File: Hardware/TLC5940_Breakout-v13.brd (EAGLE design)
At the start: 59.7 x 26.7 mm, 51 parts, among them U1 TLC5940-RHB, U2 V_REG_MIC52055V

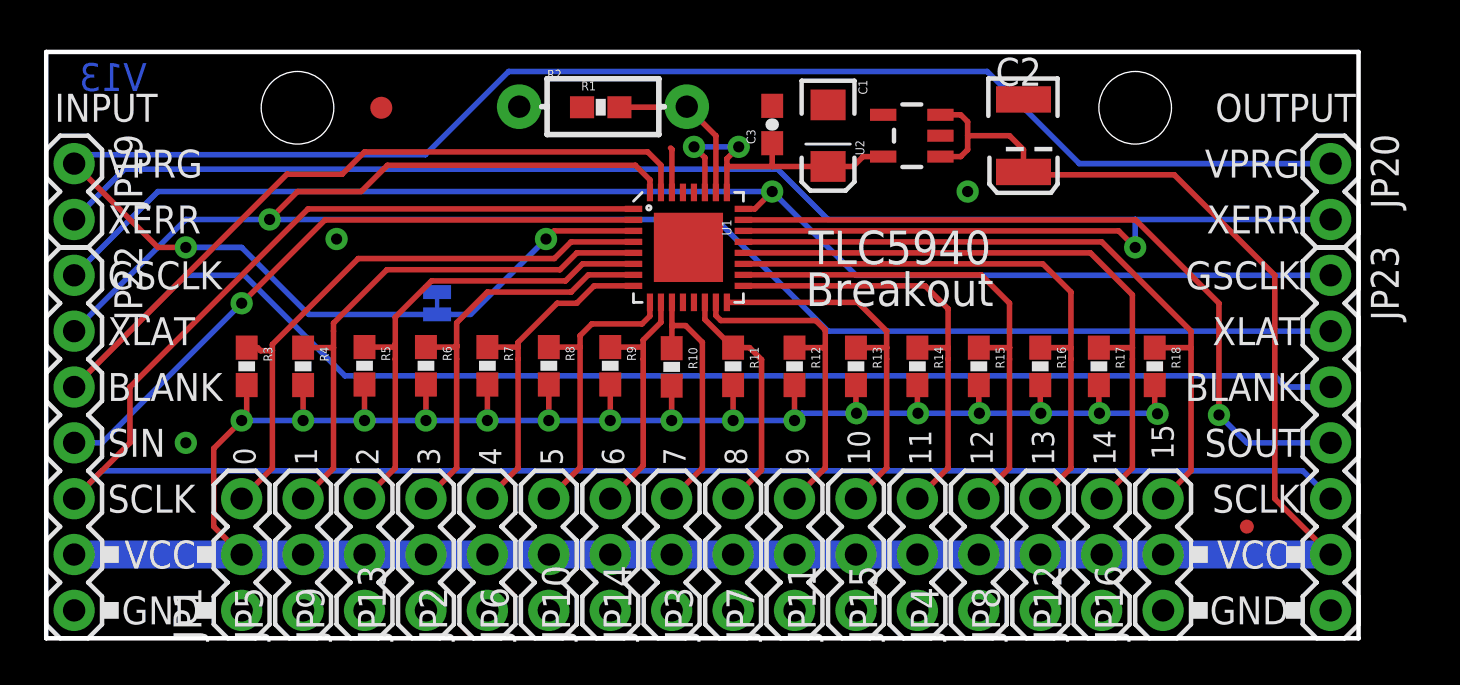
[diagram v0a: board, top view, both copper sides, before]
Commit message: Fixed sch issues, updated to 0603, minor re routes.
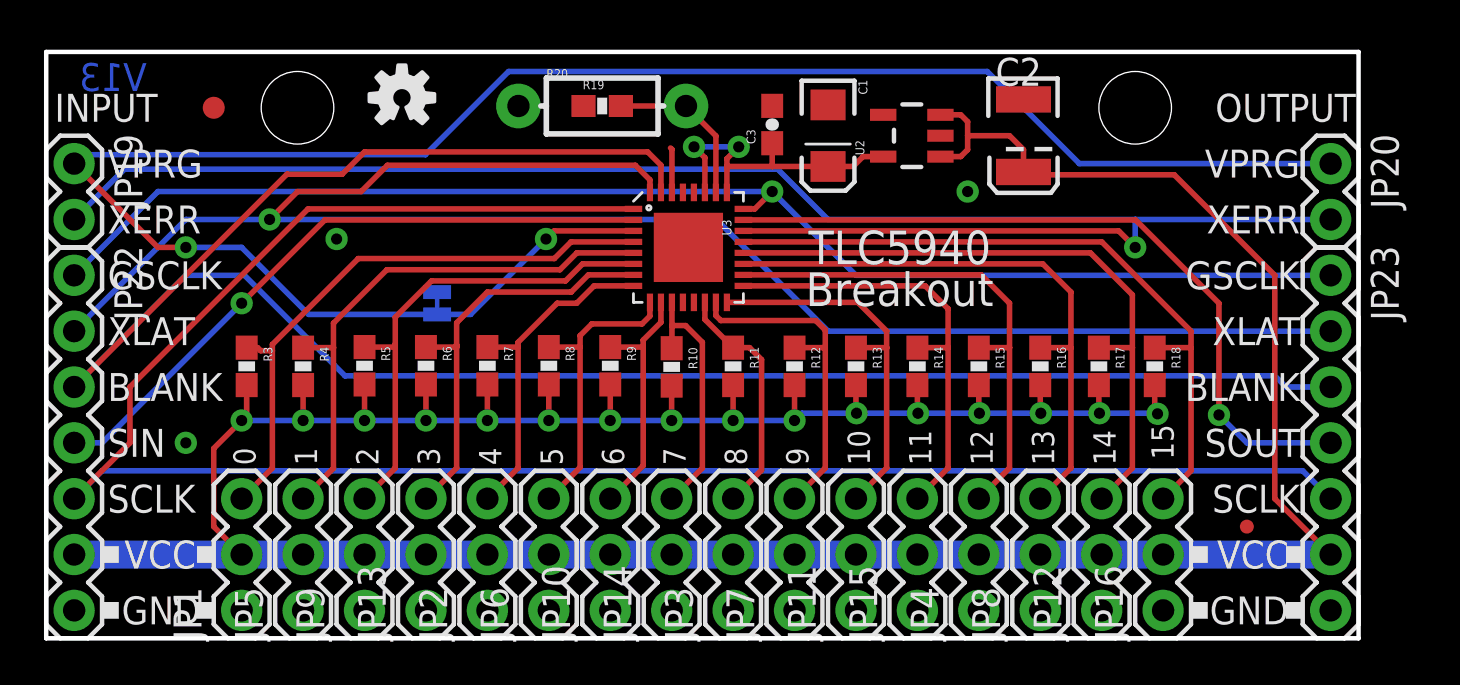
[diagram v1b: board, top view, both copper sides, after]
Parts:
- removed R1: 2.2k, SparkFun-Resistors:0603-RES
- removed R2: R2, SparkFun-Resistors:AXIAL-0.3-KIT
- removed U1: TLC5940-RHB, SparkFun:QFN-32
- added R19: 2.2k, SparkFun-Resistors:0603-RES
- added R20: R2, SparkFun-Resistors:AXIAL-0.3-KIT
- added U3: TLC5940-RHB, SparkFun-DigitalIC:QFN-32
- moved LOGO1 41.3 mm to (16.2, 24.6), flipped to the top
- moved JP26 7.62 mm to (7.62, 24.1)
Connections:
- removed net N$8: R1.2, R2.P$2, U1.26
- new net N$1: R19.2, R20.P$2, U3.26
- net 5V: now also U3.25, U3.27; no longer U1.25, U1.27
- net BLANK: now also U3.31; no longer U1.31
- net GND: now also R19.1, R20.P$1, U3.30; no longer R1.1, R2.P$1, U1.30
- net GSCLK: now also U3.24; no longer U1.24
- net OUT0: now also U3.4; no longer U1.4
- net OUT1: now also U3.5; no longer U1.5
- net OUT10: now also U3.16; no longer U1.16
- net OUT11: now also U3.17; no longer U1.17
- net OUT12: now also U3.18; no longer U1.18
- net OUT13: now also U3.19; no longer U1.19
- net OUT14: now also U3.20; no longer U1.20
- net OUT15: now also U3.21; no longer U1.21
- net OUT2: now also U3.6; no longer U1.6
- net OUT3: now also U3.7; no longer U1.7
- net OUT4: now also U3.8; no longer U1.8
- net OUT5: now also U3.9; no longer U1.9
- net OUT6: now also U3.10; no longer U1.10
- net OUT7: now also U3.11; no longer U1.11
- net OUT8: now also U3.14; no longer U1.14
- net OUT9: now also U3.15; no longer U1.15
- net SCLK: now also U3.1; no longer U1.1
- net SIN: now also U3.2; no longer U1.2
- net SOUT: now also U3.23; no longer U1.23
- net VPRG: now also U3.3; no longer U1.3
- net XERR: now also U3.22; no longer U1.22
- net XLAT: now also U3.32; no longer U1.32
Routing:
- net N$8: track 7.52 -> 0.00 mm
- net N$1: track 0.00 -> 7.46 mm

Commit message: Fixed QC Checklist issues
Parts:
- removed JP27: FIDUCIAL1X2.5, abes:FIDUCIAL-1X2.5
- added JP21: FIDUCIAL1X2, SparkFun:FIDUCIAL-1X2
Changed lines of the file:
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@@
 <setting verticaltext="up"/>
 </settings>
-<grid distance="0.05" unitdist="inch" unit="inch" style="lines" multiple="1" display="yes" altdistance="0.0001" altunitdist="inch" altunit="inch"/>
+<grid distance="0.05" unitdist="inch" unit="inch" style="lines" multiple="1" display="yes" altdistance="0.005" altunitdist="inch" altunit="inch"/>
 <layers>
 <layer number="1" name="Top" color="4" fill="1" visible="yes" active="yes"/>
@@
 <layer number="45" name="Holes" color="7" fill="1" visible="yes" active="yes"/>
 <layer number="46" name="Milling" color="3" fill="1" visible="no" active="yes"/>
-<layer number="47" name="Measures" color="7" fill="1" visible="yes" active="yes"/>
+<layer number="47" name="Measures" color="7" fill="1" visible="no" active="yes"/>
 <layer number="48" name="Document" color="7" fill="1" visible="no" active="yes"/>
 <layer number="49" name="Reference" color="7" fill="1" visible="no" active="yes"/>
@@
 <layer number="56" name="wert" color="7" fill="1" visible="no" active="yes"/>
 <layer number="57" name="tCAD" color="7" fill="1" visible="no" active="no"/>
+<layer number="59" name="tCarbon" color="7" fill="1" visible="no" active="no"/>
+<layer number="60" name="bCarbon" color="7" fill="1" visible="no" active="no"/>
 <layer number="90" name="Modules" color="5" fill="1" visible="no" active="yes"/>
 <layer number="91" name="Nets" color="2" fill="1" visible="no" active="no"/>
@@
 <layer number="127" name="_tValues" color="7" fill="1" visible="no" active="yes"/>
 <layer number="128" name="_bValues" color="7" fill="1" visible="no" active="yes"/>
+<layer number="129" name="Mask" color="7" fill="1" visible="yes" active="yes"/>
 <layer number="131" name="tAdjust" color="7" fill="1" visible="no" active="yes"/>
 <layer number="132" name="bAdjust" color="7" fill="1" visible="no" active="yes"/>
@@
 <layer number="223" name="223bmp" color="24" fill="1" visible="no" active="no"/>
 <layer number="224" name="224bmp" color="25" fill="1" visible="no" active="no"/>
+<layer number="225" name="225bmp" color="7" fill="1" visible="yes" active="yes"/>
+<layer number="226" name="226bmp" color="7" fill="1" visible="yes" active="yes"/>
+<layer number="227" name="227bmp" color="7" fill="1" visible="yes" active="yes"/>
+<layer number="228" name="228bmp" color="7" fill="1" visible="yes" active="yes"/>
+<layer number="229" name="229bmp" color="7" fill="1" visible="yes" active="yes"/>
+<layer number="230" name="230bmp" color="7" fill="1" visible="yes" active="yes"/>
+<layer number="231" name="231bmp" color="7" fill="1" visible="yes" active="yes"/>
 <layer number="248" name="Housing" color="7" fill="1" visible="no" active="yes"/>
 <layer number="249" name="Edge" color="7" fill="1" visible="no" active="yes"/>
@@
 </element>
 <element name="JP26" library="SparkFun" package="FIDUCIAL-1X2" value="FIDUCIAL1X2" x="7.62" y="24.13"/>
-<element name="JP27" library="abes" package="FIDUCIAL-1X2.5" value="FIDUCIAL1X2.5" x="54.61" y="5.08"/>
 <element name="FRAME1" library="SparkFun-Aesthetics" package="CREATIVE_COMMONS" value="FRAME-LETTER" x="-2.54" y="-16.51"/>
 <element name="LOGO1" library="SparkFun-Aesthetics" package="OSHW-LOGO-S" value="OSHW-LOGOS" x="16.1798" y="24.5872"/>
@@
 <attribute name="NAME" x="22.748240625" y="25.48128125" size="0.4064" layer="25" font="vector"/>
 </element>
+<element name="JP21" library="SparkFun" package="FIDUCIAL-1X2" value="FIDUCIAL1X2" x="54.61" y="5.08"/>
 </elements>
 <signals>
@@
 <contactref element="R3" pad="1"/>
 <wire x1="8.89" y1="6.35" x2="10.287" y2="7.747" width="0.254" layer="1"/>
-<wire x1="10.287" y1="7.747" x2="10.287" y2="13.081" width="0.254" layer="1"/>
-<wire x1="10.287" y1="13.081" x2="10.287" y2="13.365" width="0.254" layer="1"/>
+<wire x1="10.287" y1="7.747" x2="10.287" y2="12.7" width="0.254" layer="1"/>
+<wire x1="10.287" y1="13.2198" x2="10.287" y2="13.365" width="0.254" layer="1"/>
 <wire x1="23.872" y1="18.03" x2="26.71" y2="18.03" width="0.254" layer="1"/>
 <wire x1="23.114" y1="17.272" x2="23.872" y2="18.03" width="0.254" layer="1"/>
 <wire x1="14.194" y1="17.272" x2="23.114" y2="17.272" width="0.254" layer="1"/>
-<wire x1="9.1186" y1="13.2198" x2="9.6148" y2="13.2198" width="0.254" layer="1"/>
-<wire x1="9.6148" y1="13.2198" x2="9.7536" y2="13.081" width="0.254" layer="1"/>
-<wire x1="9.7536" y1="13.081" x2="10.287" y2="13.081" width="0.254" layer="1"/>
 <wire x1="10.287" y1="13.365" x2="14.194" y2="17.272" width="0.254" layer="1"/>
 <contactref element="U3" pad="4"/>
+<wire x1="9.1186" y1="13.2198" x2="10.287" y2="13.2198" width="0.254" layer="1"/>
+<wire x1="10.287" y1="13.2198" x2="10.287" y2="12.7" width="0.254" layer="1"/>
 </signal>
 <signal name="OUT2">
@@
 </signal>
 </signals>
-<errors>
-</errors>
 </board>
 </drawing>
